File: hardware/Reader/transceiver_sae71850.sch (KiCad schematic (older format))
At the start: 17 parts, among them IC8 LM317LDR2G

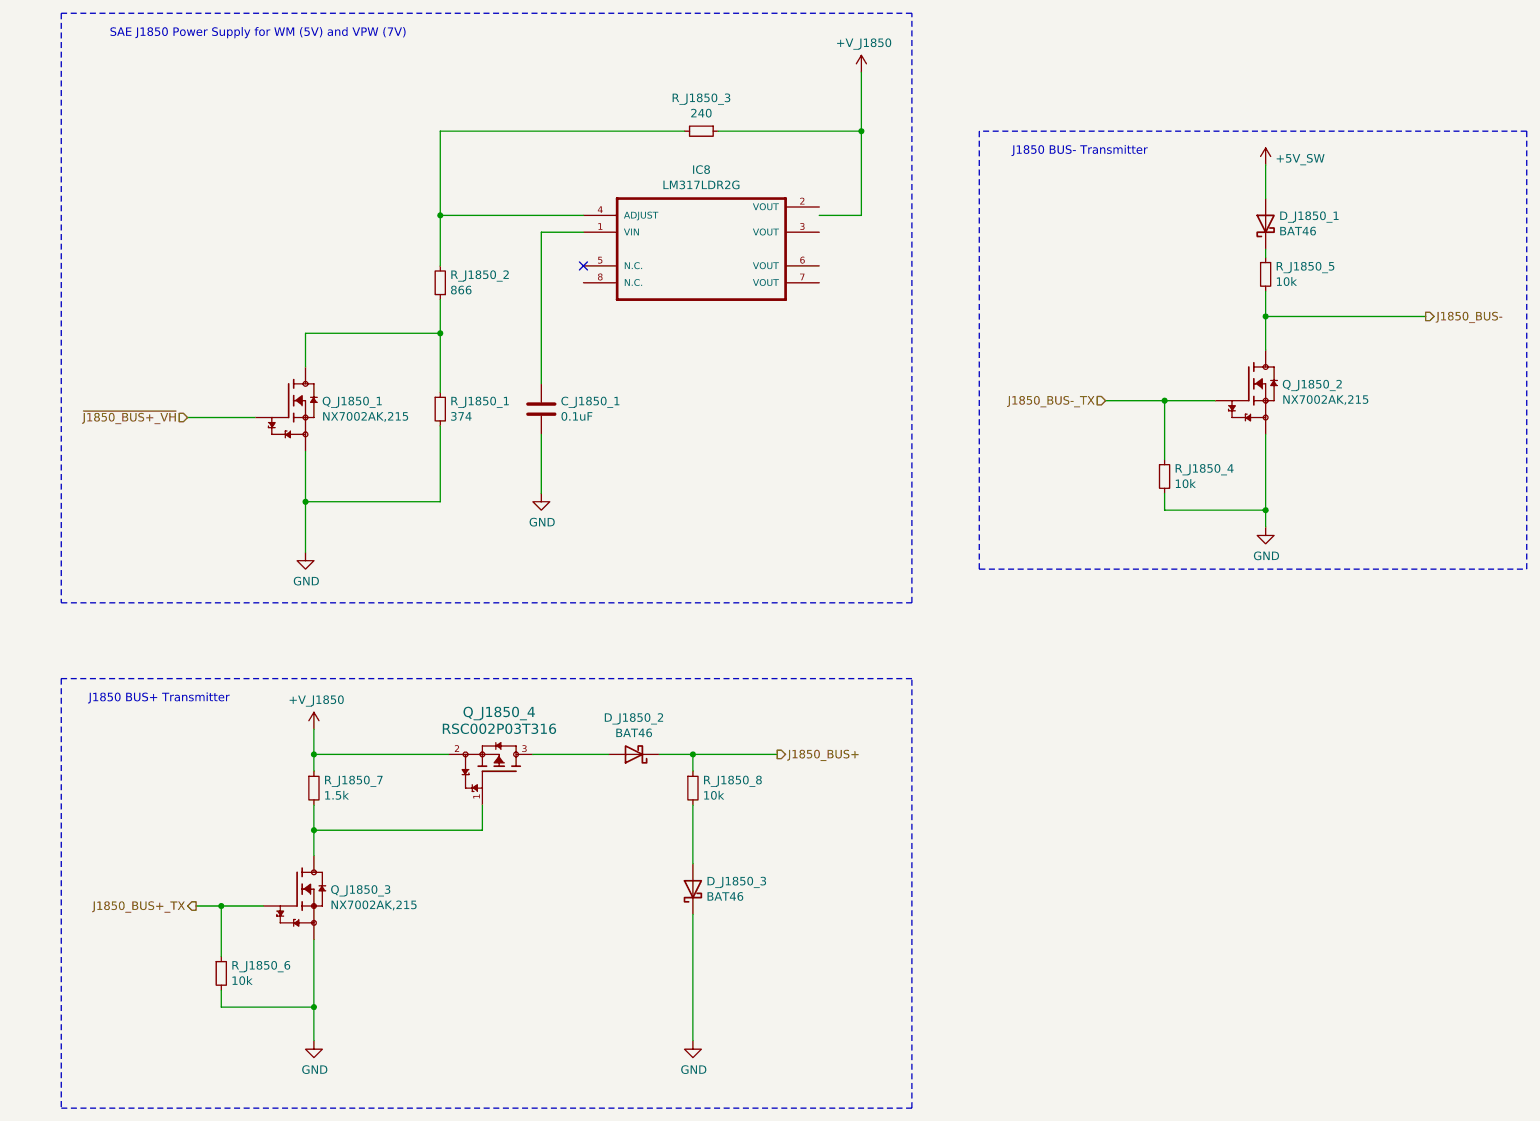
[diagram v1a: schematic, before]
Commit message: Added ESD Protection. Fixed minor bugs on schematic. Attempted placement of components
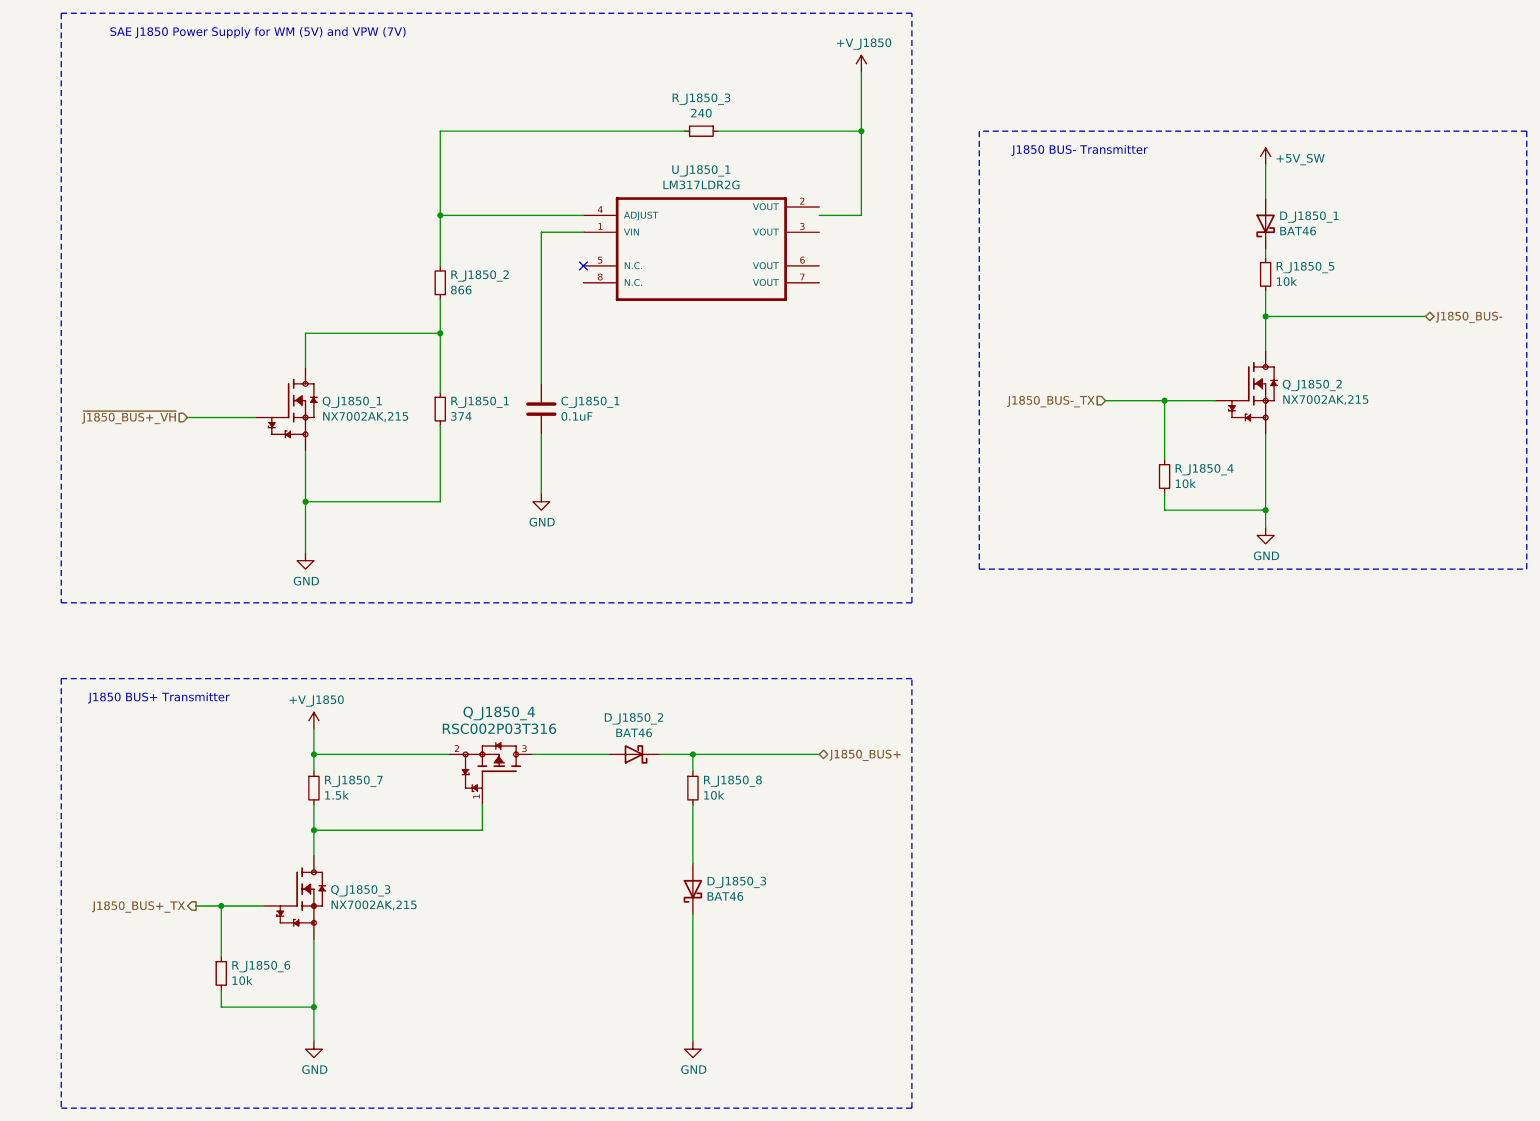
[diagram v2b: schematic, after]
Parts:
- renumbered IC8 to U_J1850_1
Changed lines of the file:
@@
 $Descr USLetter 11000 8500
 encoding utf-8
-Sheet 12 18
+Sheet 7 19
 Title "CANnect Reader | SAE J1850 VPW/PWM Transceiver"
-Date "2020-10-20"
-Rev "0.0.01"
+Date "2020-10-25"
+Rev "0.0.03"
 Comp "CANtech"
 Comment1 "Created by Choong Jin Ng | jin8383@gmail.com"
@@
 $EndDescr
 $Comp
-L LM317LDR2G:LM317LDR2G IC8
+L LM317LDR2G:LM317LDR2G U_J1850_1
 U 1 1 5FB525E1
 P 4450 2100
-F 0 "IC8" H 4450 2570 50  0000 C CNN
+F 0 "U_J1850_1" H 4450 2570 50  0000 C CNN
 F 1 "LM317LDR2G" H 4450 2479 50  0000 C CNN
 F 2 "footprints:SOIC127P600X175-8N" H 4450 2100 50  0001 L BNN
@@
 Wire Wire Line
 	3450 5100 3900 5100
-Text HLabel 4900 5100 2    50   Output ~ 0
+Text HLabel 5150 5100 2    50   BiDi ~ 0
 J1850_BUS+
 Wire Wire Line
@@
 	4400 5200 4400 5100
 Connection ~ 4400 5100
-Wire Wire Line
-	4400 5100 4900 5100
 Wire Wire Line
 	4400 5400 4400 5750
@@
 	0    -1   -1   0
 $EndComp
-Text HLabel 8750 2500 2    50   Output ~ 0
+Text HLabel 8750 2500 2    50   BiDi ~ 0
 J1850_BUS-
 Wire Wire Line
@@
 Wire Wire Line
 	7800 2150 7800 2100
-Wire Wire Line
-	8750 2500 7800 2500
 Connection ~ 7800 2500
 Wire Wire Line
@@
 Wire Wire Line
 	1600 6000 1850 6000
+Wire Wire Line
+	7800 2500 8750 2500
+Wire Wire Line
+	4400 5100 5150 5100
 $EndSCHEMATC

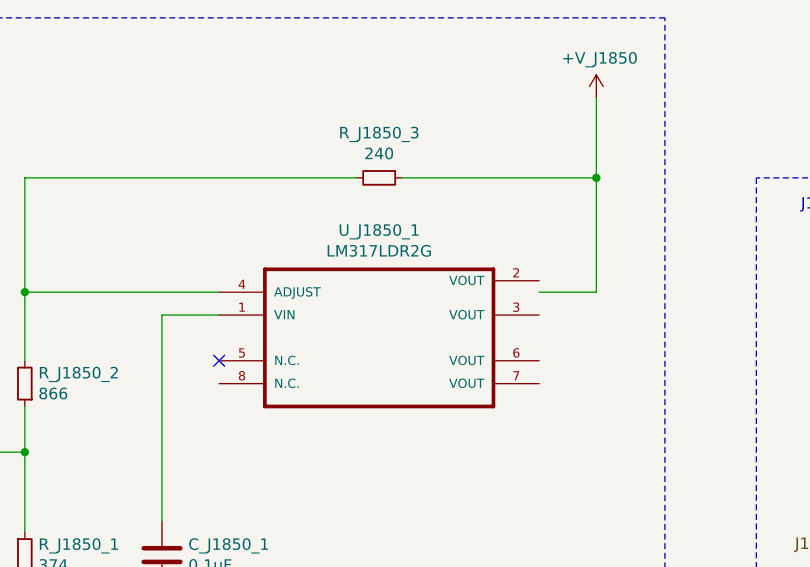
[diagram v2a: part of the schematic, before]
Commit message: Fixed bugs on the reader schematic. Exported Schematic Electrical report
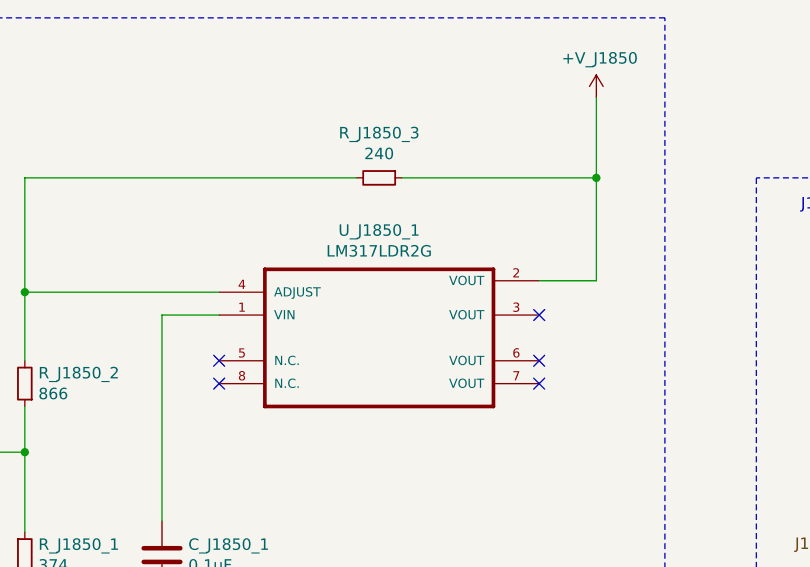
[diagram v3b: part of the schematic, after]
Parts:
- C_J1850_1: Manufacturer (none) -> Yageo; Part Name (none) -> CC0603JRX7R8BB104; Vendor (none) -> DigiKey Canada; digikeypn (none) -> 311-1777-1-ND
- D_J1850_1, D_J1850_2, D_J1850_3: Manufacturer (none) -> STMicroelectronics; Part Name (none) -> BAT46; Vendor (none) -> DigiKey Canada; digikeypn (none) -> 497-3768-1-ND
- Q_J1850_1, Q_J1850_2, Q_J1850_3: Manufacturer (none) -> Nexperia USA Inc.; Part Name (none) -> NX7002AK,215; Vendor (none) -> DigiKey Canada; digikeypn (none) -> 1727-1289-1-ND
- Q_J1850_4: Manufacturer (none) -> Rohm Semiconductor; Part Name (none) -> RSC002P03T316; Vendor (none) -> DigiKey Canada; digikeypn (none) -> RSC002P03T316CT-ND
- R_J1850_1: Manufacturer (none) -> Panasonic Electronic Components; Vendor (none) -> DigiKey Canada; digikeypn (none) -> P374FCT-ND
- R_J1850_2: Manufacturer (none) -> Panasonic Electronic Components; Vendor (none) -> DigiKey Canada; digikeypn (none) -> P866FCT-ND
- R_J1850_3: Manufacturer (none) -> Panasonic Electronic Components; Vendor (none) -> DigiKey Canada; digikeypn (none) -> P240FCT-ND
- R_J1850_4, R_J1850_5, R_J1850_6, R_J1850_8: Manufacturer (none) -> Yageo; Vendor (none) -> DigiKey Canada; digikeypn (none) -> YAG2321CT-ND
- R_J1850_7: Manufacturer (none) -> Yageo; Vendor (none) -> DigiKey Canada; digikeypn (none) -> 311-1.50KHRCT-ND
- U_J1850_1: Manufacturer (none) -> ON Semiconductor; Part Name (none) -> LM317LDR2G; Vendor (none) -> DigiKey Canada; digikeypn (none) -> LM317LDR2GOSCT-ND
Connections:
- net +V_J1850: now also U_J1850_1.2 (VOUT)
- no-connect marks 1 -> 5
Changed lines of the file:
@@
 F 2 "footprints:SOIC127P600X175-8N" H 4450 2100 50  0001 L BNN
 F 3 "https://www.onsemi.com/pub/Collateral/LM317L-D.PDF" H 4450 2100 50  0001 C CNN
+F 4 "LM317LDR2G" H 4450 2100 50  0001 C CNN "Part Name"
+F 5 "ON Semiconductor" H 4450 2100 50  0001 C CNN "Manufacturer"
+F 6 "DigiKey Canada" H 4450 2100 50  0001 C CNN "Vendor"
+F 7 "LM317LDR2GOSCT-ND" H 4450 2100 50  0001 C CNN "digikeypn"
 	1    4450 2100
 	1    0    0    -1
@@
 F 2 "footprints:CAPC1608X90" H 3538 2900 50  0001 C CNN
 F 3 "https://www.yageo.com/upload/media/product/productsearch/datasheet/mlcc/UPY-GPHC_X7R_6.3V-to-50V_18.pdf" H 3500 3050 50  0001 C CNN
+F 4 "CC0603JRX7R8BB104" H 3500 3050 50  0001 C CNN "Part Name"
+F 5 "Yageo" H 3500 3050 50  0001 C CNN "Manufacturer"
+F 6 "DigiKey Canada" H 3500 3050 50  0001 C CNN "Vendor"
+F 7 "311-1777-1-ND" H 3500 3050 50  0001 C CNN "digikeypn"
 	1    3500 3050
 	1    0    0    -1
@@
 F 3 "https://industrial.panasonic.com/cdbs/www-data/pdf/RDA0000/AOA0000C304.pdf" H 4450 1400 50  0001 C CNN
 F 4 "ERJ-8ENF2400V" H 4450 1400 50  0001 C CNN "Part Name"
+F 5 "DigiKey Canada" H 4450 1400 50  0001 C CNN "Vendor"
+F 6 "Panasonic Electronic Components" H 4450 1400 50  0001 C CNN "Manufacturer"
+F 7 "P240FCT-ND" H 4450 1400 50  0001 C CNN "digikeypn"
 	1    4450 1400
 	0    1    1    0
@@
 F 3 "https://industrial.panasonic.com/cdbs/www-data/pdf/RDA0000/AOA0000C304.pdf" H 2900 2300 50  0001 C CNN
 F 4 "ERJ-8ENF8660V" H 2900 2300 50  0001 C CNN "Part Name"
+F 5 "DigiKey Canada" H 2900 2300 50  0001 C CNN "Vendor"
+F 6 "Panasonic Electronic Components" H 2900 2300 50  0001 C CNN "Manufacturer"
+F 7 "P866FCT-ND" H 2900 2300 50  0001 C CNN "digikeypn"
 	1    2900 2300
 	-1   0    0    1
@@
 F 5 "7" H 2000 3000 50  0001 L BNN "Field5"
 F 6 "IPC-7351B" H 2000 3000 50  0001 L BNN "Field6"
+F 7 "NX7002AK,215" H 2000 3000 50  0001 C CNN "Part Name"
+F 8 "Nexperia USA Inc." H 2000 3000 50  0001 C CNN "Manufacturer"
+F 9 "DigiKey Canada" H 2000 3000 50  0001 C CNN "Vendor"
+F 10 "1727-1289-1-ND" H 2000 3000 50  0001 C CNN "digikeypn"
 	1    2000 3000
 	1    0    0    -1
@@
 F 3 "https://industrial.panasonic.com/cdbs/www-data/pdf/RDA0000/AOA0000C304.pdf" H 2900 3050 50  0001 C CNN
 F 4 "ERJ-8ENF3740V" H 2900 3050 50  0001 C CNN "Part Name"
+F 5 "DigiKey Canada" H 2900 3050 50  0001 C CNN "Vendor"
+F 6 "Panasonic Electronic Components" H 2900 3050 50  0001 C CNN "Manufacturer"
+F 7 "P374FCT-ND" H 2900 3050 50  0001 C CNN "digikeypn"
 	1    2900 3050
 	1    0    0    -1
@@
 Wire Wire Line
 	4550 1400 5400 1400
-Connection ~ 5400 1400
-Wire Wire Line
-	5400 1400 5400 1900
-Wire Wire Line
-	5150 1900 5400 1900
 Wire Notes Line
 	650  4200 5700 4200
@@
 F 5 "7" H 2050 5900 50  0001 L BNN "Field5"
 F 6 "IPC-7351B" H 2050 5900 50  0001 L BNN "Field6"
+F 7 "NX7002AK,215" H 2050 5900 50  0001 C CNN "Part Name"
+F 8 "Nexperia USA Inc." H 2050 5900 50  0001 C CNN "Manufacturer"
+F 9 "DigiKey Canada" H 2050 5900 50  0001 C CNN "Vendor"
+F 10 "1727-1289-1-ND" H 2050 5900 50  0001 C CNN "digikeypn"
 	1    2050 5900
 	1    0    0    -1
@@
 F 2 "footprints:RSC002P03T316" H 3800 5690 60  0001 C CNN
 F 3 "http://rohmfs.rohm.com/en/products/databook/datasheet/discrete/transistor/mosfet/rsc002p03-e.pdf" H 3800 5731 60  0001 C CNN
+F 4 "RSC002P03T316" H 3000 5450 50  0001 C CNN "Part Name"
+F 5 "DigiKey Canada" H 3000 5450 50  0001 C CNN "Vendor"
+F 6 "Rohm Semiconductor" H 3000 5450 50  0001 C CNN "Manufacturer"
+F 7 "RSC002P03T316CT-ND" H 3000 5450 50  0001 C CNN "digikeypn"
 	1    3000 5450
 	0    1    -1   0
@@
 F 3 "https://www.yageo.com/upload/media/product/productsearch/datasheet/rchip/PYu-RC_Group_51_RoHS_L_11.pdf" H 2150 5300 50  0001 C CNN
 F 4 "RC0603FR-071K5L" H 2150 5300 50  0001 C CNN "Part Name"
+F 5 "Yageo" H 2150 5300 50  0001 C CNN "Manufacturer"
+F 6 "DigiKey Canada" H 2150 5300 50  0001 C CNN "Vendor"
+F 7 "311-1.50KHRCT-ND" H 2150 5300 50  0001 C CNN "digikeypn"
 	1    2150 5300
 	1    0    0    -1
@@
 F 3 "https://www.yageo.com/upload/media/product/productsearch/datasheet/rchip/PYu-RT_1-to-0.01_RoHS_L_12.pdf" H 1600 6400 50  0001 C CNN
 F 4 "RT0603FRE0710KL" H 1600 6400 50  0001 C CNN "Part Name"
+F 5 "Yageo" H 1600 6400 50  0001 C CNN "Manufacturer"
+F 6 "DigiKey Canada" H 1600 6400 50  0001 C CNN "Vendor"
+F 7 "YAG2321CT-ND" H 1600 6400 50  0001 C CNN "digikeypn"
 	1    1600 6400
 	1    0    0    -1
@@
 F 2 "Diode_THT:D_DO-35_SOD27_P7.62mm_Horizontal" H 4050 4925 50  0001 C CNN
 F 3 "http://www.vishay.com/docs/85662/bat46.pdf" H 4050 5100 50  0001 C CNN
+F 4 "BAT46" H 4050 5100 50  0001 C CNN "Part Name"
+F 5 "STMicroelectronics" H 4050 5100 50  0001 C CNN "Manufacturer"
+F 6 "DigiKey Canada" H 4050 5100 50  0001 C CNN "Vendor"
+F 7 "497-3768-1-ND" H 4050 5100 50  0001 C CNN "digikeypn"
 	1    4050 5100
 	-1   0    0    1
@@
 F 3 "https://www.yageo.com/upload/media/product/productsearch/datasheet/rchip/PYu-RT_1-to-0.01_RoHS_L_12.pdf" H 4400 5300 50  0001 C CNN
 F 4 "RT0603FRE0710KL" H 4400 5300 50  0001 C CNN "Part Name"
+F 5 "Yageo" H 4400 5300 50  0001 C CNN "Manufacturer"
+F 6 "DigiKey Canada" H 4400 5300 50  0001 C CNN "Vendor"
+F 7 "YAG2321CT-ND" H 4400 5300 50  0001 C CNN "digikeypn"
 	1    4400 5300
 	1    0    0    -1
@@
 F 2 "Diode_THT:D_DO-35_SOD27_P7.62mm_Horizontal" H 4400 5725 50  0001 C CNN
 F 3 "http://www.vishay.com/docs/85662/bat46.pdf" H 4400 5900 50  0001 C CNN
+F 4 "BAT46" H 4400 5900 50  0001 C CNN "Part Name"
+F 5 "STMicroelectronics" H 4400 5900 50  0001 C CNN "Manufacturer"
+F 6 "DigiKey Canada" H 4400 5900 50  0001 C CNN "Vendor"
+F 7 "497-3768-1-ND" H 4400 5900 50  0001 C CNN "digikeypn"
 	1    4400 5900
 	0    -1   -1   0
@@
 F 5 "7" H 7700 2900 50  0001 L BNN "Field5"
 F 6 "IPC-7351B" H 7700 2900 50  0001 L BNN "Field6"
+F 7 "NX7002AK,215" H 7700 2900 50  0001 C CNN "Part Name"
+F 8 "Nexperia USA Inc." H 7700 2900 50  0001 C CNN "Manufacturer"
+F 9 "DigiKey Canada" H 7700 2900 50  0001 C CNN "Vendor"
+F 10 "1727-1289-1-ND" H 7700 2900 50  0001 C CNN "digikeypn"
 	1    7700 2900
 	1    0    0    -1
@@
 F 3 "https://www.yageo.com/upload/media/product/productsearch/datasheet/rchip/PYu-RT_1-to-0.01_RoHS_L_12.pdf" H 7200 3450 50  0001 C CNN
 F 4 "RT0603FRE0710KL" H 7200 3450 50  0001 C CNN "Part Name"
+F 5 "Yageo" H 7200 3450 50  0001 C CNN "Manufacturer"
+F 6 "DigiKey Canada" H 7200 3450 50  0001 C CNN "Vendor"
+F 7 "YAG2321CT-ND" H 7200 3450 50  0001 C CNN "digikeypn"
 	1    7200 3450
 	1    0    0    -1
@@
 F 3 "https://www.yageo.com/upload/media/product/productsearch/datasheet/rchip/PYu-RT_1-to-0.01_RoHS_L_12.pdf" H 7800 2250 50  0001 C CNN
 F 4 "RT0603FRE0710KL" H 7800 2250 50  0001 C CNN "Part Name"
+F 5 "Yageo" H 7800 2250 50  0001 C CNN "Manufacturer"
+F 6 "DigiKey Canada" H 7800 2250 50  0001 C CNN "Vendor"
+F 7 "YAG2321CT-ND" H 7800 2250 50  0001 C CNN "digikeypn"
 	1    7800 2250
 	1    0    0    -1
@@
 F 2 "Diode_THT:D_DO-35_SOD27_P7.62mm_Horizontal" H 7800 1775 50  0001 C CNN
 F 3 "http://www.vishay.com/docs/85662/bat46.pdf" H 7800 1950 50  0001 C CNN
+F 4 "BAT46" H 7800 1950 50  0001 C CNN "Part Name"
+F 5 "STMicroelectronics" H 7800 1950 50  0001 C CNN "Manufacturer"
+F 6 "DigiKey Canada" H 7800 1950 50  0001 C CNN "Vendor"
+F 7 "497-3768-1-ND" H 7800 1950 50  0001 C CNN "digikeypn"
 	1    7800 1950
 	0    -1   -1   0
@@
 Text Notes 7100 1550 2    50   ~ 0
 J1850 BUS- Transmitter
-NoConn ~ 3750 2200
 Wire Wire Line
 	3500 2000 3750 2000
@@
 Wire Wire Line
 	4400 5100 5150 5100
+NoConn ~ 3750 2200
+NoConn ~ 3750 2300
+NoConn ~ 5150 2000
+NoConn ~ 5150 2200
+NoConn ~ 5150 2300
+Wire Wire Line
+	5400 1400 5400 1850
+Wire Wire Line
+	5400 1850 5150 1850
+Connection ~ 5400 1400
 $EndSCHEMATC
